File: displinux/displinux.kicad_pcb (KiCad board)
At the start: 2 copper layers, 57.9 x 65.4 mm, 146 parts, among them J1 USB4105-GF-A, J10 Conn_01x03, J2 USB4105-GF-A, J3 AudioJack4, J4 Conn_02x10_Counter_Clockwise, J5 HR911105A, J6 Conn_01x24_MountingPin, J7 Conn_01x06, J8 Conn_01x40_MountingPin, J9 Conn_01x02_Pin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

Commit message: add fixes
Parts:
- removed R33: 0, Resistor_SMD:R_0603_1608Metric
- removed R47, R48: 10k, Resistor_SMD:R_0603_1608Metric
- added C13: 10u, Capacitor_SMD:C_0603_1608Metric, B.Cu at (247.4, 98.7)
- C40, C44: value 0.1u -> 10u
- D5: footprint Diode_SMD:D_0805_2012Metric -> Diode_SMD:D_2010_5025Metric
- moved U7 2.10 mm to (241.2, 106.8)
- moved C53 1.84 mm to (238.4, 106.9)
- moved C54 1.68 mm to (238.5, 103.3)
- moved R41 1.56 mm to (244.3, 98.8)
- moved L3 1.03 mm to (242.0, 103.0)
- moved D5 0.55 mm to (245.5, 102.9)
- moved C41 0.39 mm to (235.9, 96.6)
- moved C51 0.10 mm to (251.1, 91.4)
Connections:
- J8 pad 31: /DISP -> +3V3
- U3 pad 91: Net-(U3-AGND) -> GND
- U8 pad 9: GND -> (no net)
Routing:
- net GND: track 148.6 -> 180.1 mm, vias 122 -> 127
- net /LCD_A: track 13.0 -> 18.1 mm, vias 2 -> 3
- net Net-(U3-AGND): track 3.36 -> 0.00 mm
- net /DISP: track 2.86 -> 0.00 mm, vias 1 -> 0
- net Net-(U3-DZQ): track 2.68 -> 1.17 mm
- net /LCD_K: track 7.29 -> 6.20 mm
- net +5V: track 189.5 -> 190.5 mm
- net /LCD0_PWM: track 14.1 -> 14.9 mm
- net /LDOB-OUT: track 16.2 -> 15.5 mm
- net +3V3: track 338.4 -> 339.0 mm, vias 33 -> 34
- net Net-(D5-A): track 6.09 -> 6.64 mm

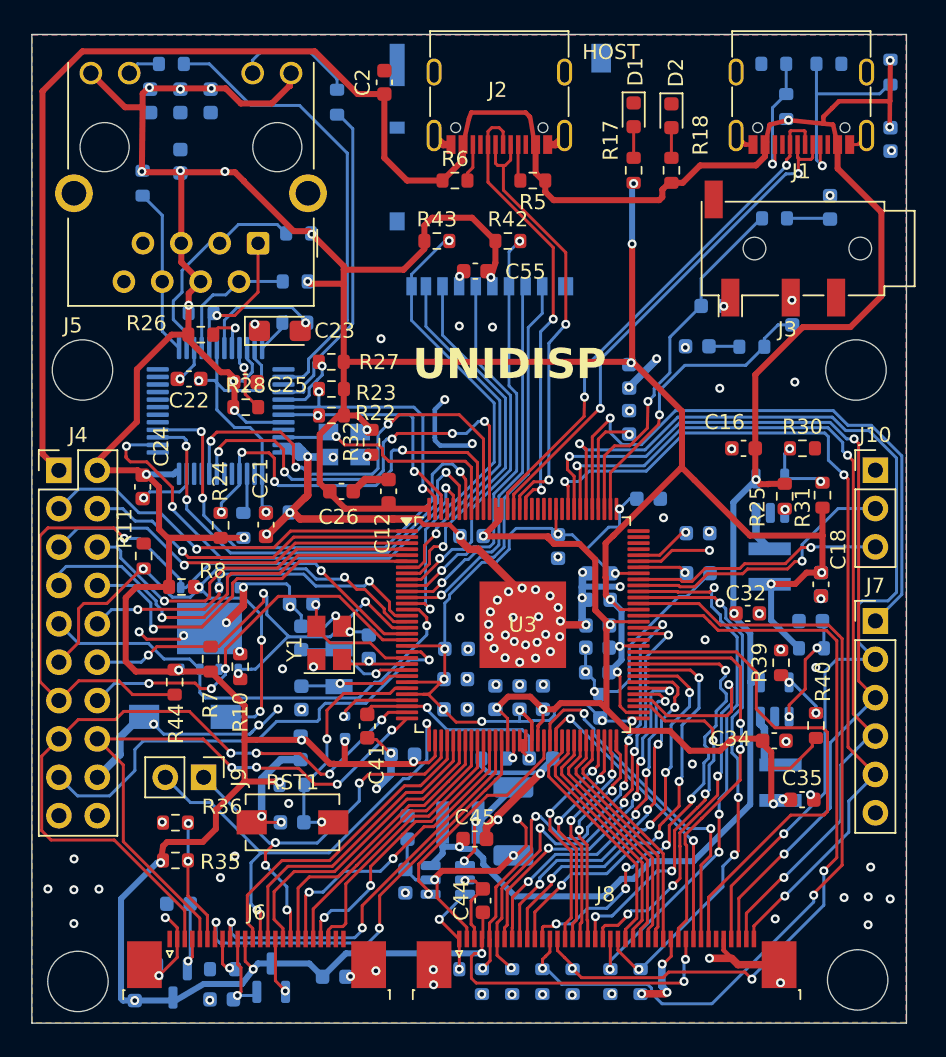
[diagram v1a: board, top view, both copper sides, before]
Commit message: fix display power
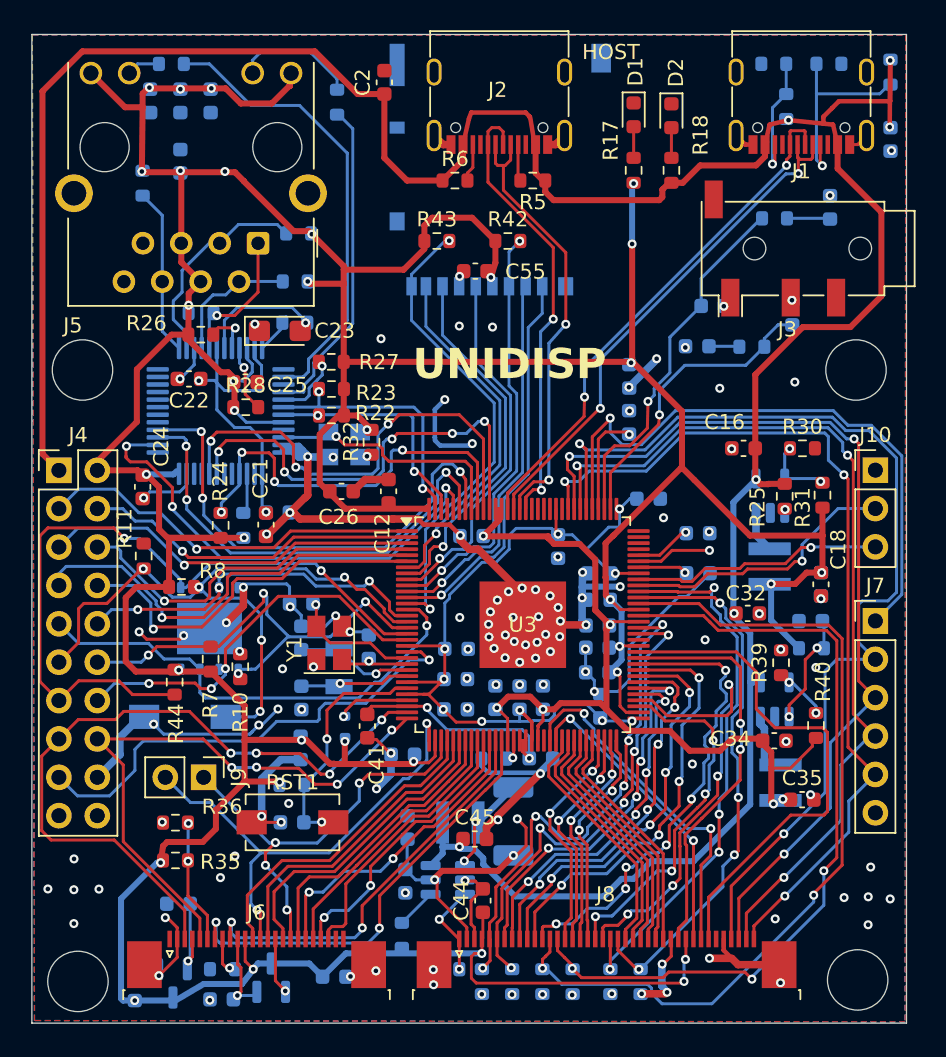
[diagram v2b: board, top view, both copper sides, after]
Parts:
- added R33: 5k, Resistor_SMD:R_0603_1608Metric, B.Cu at (238.2, 110.5)
- R46: value 2R2 -> 5R1
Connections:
- U3 pad 52: /LCD0_PWM -> unconnected-(U3-PD22-Pad52)
- U7 pad 4: /LCD0_PWM -> Net-(U7-EN/PWM)
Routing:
- net /LCD0_PWM: track 14.9 -> 0.00 mm, vias 1 -> 0
- net Net-(U7-EN/PWM): track 0.00 -> 2.69 mm

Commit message: add lvds
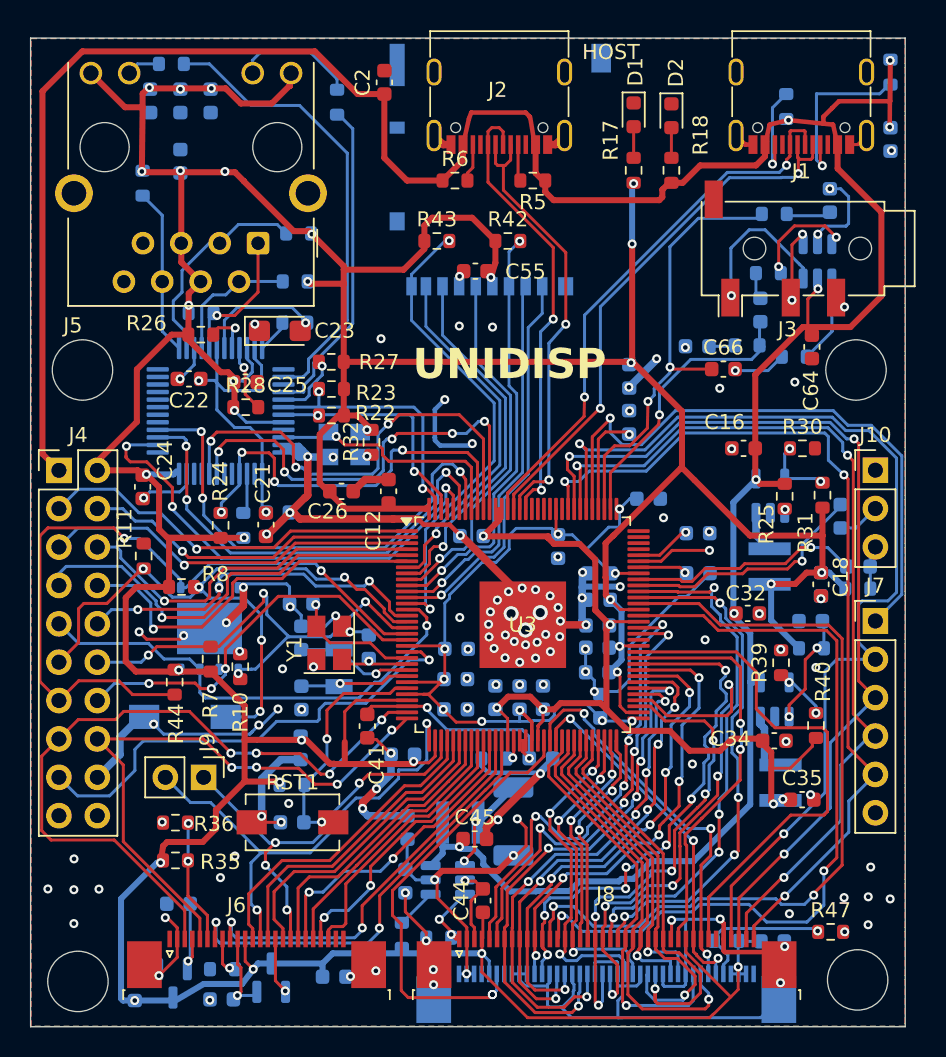
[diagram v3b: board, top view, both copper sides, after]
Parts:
- removed D3: D, Diode_SMD:D_SOD-523
- removed R1, R3: 5.1k, Resistor_SMD:R_0603_1608Metric
- removed R51, R52, R53, R54: 10k, Resistor_SMD:R_0603_1608Metric
- added C14: 10u, Capacitor_SMD:C_0603_1608Metric, B.Cu at (262.7, 110.9)
- added C64: 10u, Capacitor_SMD:C_0603_1608Metric, F.Cu at (265.3, 71.5)
- added C65: 10u, Capacitor_SMD:C_0603_1608Metric, B.Cu at (261.9, 69.1)
- added C66: 10u, Capacitor_SMD:C_0603_1608Metric, F.Cu at (259.4, 73.0)
- added J11: Conn_01x40_MountingPin, Connector_FFC-FPC:TE_4-1734839-0_1x40-1MP_P0.5mm_Horizontal, B.Cu at (251.7, 114.4)
- added R37: 10k, Resistor_SMD:R_0603_1608Metric, B.Cu at (259.6, 110.8)
- added R47: 10k, Resistor_SMD:R_0603_1608Metric, F.Cu at (266.5, 110.2)
- added R48: 150K, Resistor_SMD:R_0603_1608Metric, B.Cu at (262.4, 66.6)
- added U9: PAM8301, Package_TO_SOT_SMD:SOT-23-6, B.Cu at (265.7, 65.8)
- C37: value 0.1u -> 4.7u
- R2, R4, R5, R6: value 5.1k -> 51k
- R49: value 10k -> 150K
- R50: value 10k -> 2R2
- moved R49 46.2 mm to (264.1, 72.2), turned to 0 degrees
- moved R50 34.6 mm to (268.3, 87.5), turned to 180 degrees
- moved C4 17.3 mm to (268.4, 86.0), turned to 0 degrees
- moved C6 16.3 mm to (267.2, 82.7), turned to -90 degrees
- moved R46 2.16 mm to (240.6, 110.6)
- moved C7 0.46 mm to (266.5, 61.8)
- moved R9 0.33 mm to (261.0, 71.4)
- moved R12 0.29 mm to (262.8, 62.7)
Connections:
- C4 pad 1: Net-(C4-Pad1) -> /MIC3N
- C4 pad 2: /HPOUTR -> Net-(J10-Pin_3)
- C6 pad 1: Net-(C6-Pad1) -> /MIC3P
- C6 pad 2: /HPOUTL -> Net-(J10-Pin_2)
- J10 pad 2: /MIC3P -> Net-(J10-Pin_2)
- J10 pad 3: /MIC3N -> Net-(J10-Pin_3)
- J3 pad R1: Net-(C4-Pad1) -> Net-(U9-OUT-)
- J3 pad T: Net-(C6-Pad1) -> Net-(U9-OUT+)
- R49 pad 1: /LCD0-D16 -> Net-(C66-Pad2)
- R49 pad 2: GND -> Net-(U9-~{SD})
- R50 pad 1: /LCD0-D17 -> Net-(J10-Pin_3)
- R50 pad 2: GND -> +3V3
- U3 pad 29: Net-(D3-K) -> +3V3
- U3 pad 52: unconnected-(U3-PD22-Pad52) -> /PWM_LCD
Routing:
- net GND: track 180.1 -> 229.8 mm
- net /PWM_LCD: track 0.00 -> 29.5 mm, vias 0 -> 2
- net +3V3: track 339.0 -> 360.8 mm, vias 34 -> 32
- net /LCD0-D3: track 16.1 -> 28.3 mm, vias 0 -> 1
- net /LCD0-D18: track 25.8 -> 36.9 mm, vias 4 -> 5
- net /LCD0-D2: track 16.2 -> 27.2 mm, vias 0 -> 1
- net /LCD0-D7: track 15.6 -> 26.5 mm, vias 0 -> 1
- net /LCD0-D19: track 24.5 -> 35.1 mm, vias 4 -> 5
- net Net-(J11-Pin_5): track 0.00 -> 10.3 mm, vias 0 -> 1
- net Net-(U9-OUT+): track 0.00 -> 10.3 mm, vias 0 -> 1
- net /LCD0-D6: track 15.7 -> 25.5 mm, vias 0 -> 1
- net /LCD0-D14: track 24.5 -> 32.1 mm, vias 4 -> 5
- net /LCD0-D20: track 25.9 -> 33.3 mm, vias 4 -> 5
- net /LCD0-D10: track 15.3 -> 22.2 mm, vias 2 -> 3
- net /LCD0-D21: track 27.0 -> 33.6 mm, vias 4 -> 5
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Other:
- outline, holes or cut-outs redrawn

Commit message: some fixes
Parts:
- added R1: 10, Resistor_SMD:R_0603_1608Metric, B.Cu at (265.4, 69.6)
- added R3: 51k, Resistor_SMD:R_0603_1608Metric, B.Cu at (266.7, 53.0)
- added R51: 51k, Resistor_SMD:R_0603_1608Metric, B.Cu at (262.7, 53.0)
- C64: value 10u -> 470u
- R50: value 2R2 -> 2k
- XS1: footprint Connector_Card:microSD_HC_Hirose_DM3AT-SF-PEJM5 -> Micro_SD:J_SD_Card-micro_socket_A
- moved XS1 0.84 mm to (244.4, 59.0), turned to 180 degrees
- moved C64 0.74 mm to (265.4, 72.2)
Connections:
- C64 pad 1: +5V -> Net-(U9-VDD)
- R49 pad 2: Net-(U9-~{SD}) -> Net-(U9-IN)
- U9 pad 4: Net-(U9-~{SD}) -> Net-(U9-VDD)
- U9 pad 5: +5V -> Net-(U9-VDD)
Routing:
- net Net-(U9-IN): track 6.21 -> 12.9 mm
- net Net-(U9-~{SD}): track 5.87 -> 0.00 mm
- net Net-(U9-VDD): track 0.00 -> 5.27 mm, vias 0 -> 2
- net +5V: track 193.7 -> 190.3 mm
- net Net-(J1-CC1): track 11.5 -> 13.4 mm
- net Net-(J1-CC2): track 6.61 -> 8.41 mm
- net /SDC0-D3: track 25.2 -> 26.8 mm
- net /SDC0-D2: track 26.2 -> 27.7 mm
- net /SDC0-D0: track 24.3 -> 25.8 mm
- net /SDC0-CLK: track 24.4 -> 26.0 mm
- net /SDC0-D1: track 23.6 -> 25.1 mm
- net /SDC0-CD: track 31.5 -> 32.7 mm
- removed copper zone on B.Cu, net GND
- removed copper zone on F.Cu, net GND

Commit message: fix audio
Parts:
- added G***: LOGO, Micro_SD:logo_disp, F.Cu at (251.2, 106.5)
- added Hello Disp: LOGO, Micro_SD:linux_mascot, F.Cu at (245.1, 76.4)
- added R52: 5R1, Resistor_SMD:R_0603_1608Metric, F.Cu at (265.7, 114.7)
- added R53: 5R1, Resistor_SMD:R_0603_1608Metric, F.Cu at (265.7, 111.6)
- added R54: 0, Resistor_SMD:R_0603_1608Metric, B.Cu at (236.1, 108.2)
- R29: footprint Resistor_SMD:R_0603_1608Metric -> Resistor_SMD:R_0805_2012Metric_Pad1.20x1.40mm_HandSolder
- moved R47 1.25 mm to (267.3, 109.3)
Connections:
- J8 pad 31: +3V3 -> /DISP
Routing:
- net /DISP: track 0.00 -> 12.3 mm
- net Net-(U7-EN/PWM): track 2.69 -> 6.41 mm
- net +3V3: track 360.8 -> 362.3 mm, vias 32 -> 33
- net Net-(J11-Pin_5): track 10.3 -> 11.2 mm
- net /PWM_LCD: track 29.5 -> 29.7 mm, vias 2 -> 3
- added copper zone on B.Cu, net GND
- added copper zone on F.Cu, net GND
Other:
- board text added: "100Mbit"
- board text added: "CAM"
- board text added: "LVDS"
- board text added: "RGB24"
- board text added: "UNIxDISP"
- board text added: "X1"
- board text added: "X2"
- board text added: "Y1"
- board text added: "Y2"
- board text removed: "UNIDISP"
